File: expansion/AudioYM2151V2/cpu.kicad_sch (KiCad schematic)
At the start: 31 parts, among them J3 JTAG_68K, J4 Serial Out, U10 74LS374, U11 68008, U12 74LS374, U13 74LS148, U14 AS6C4008-55PCN, U15 AT28C256B, U16 XC9536PC44, U17 SC26C92C1A, U9 74LS374, X2 8Mhz, Y1 3.6864Mhz

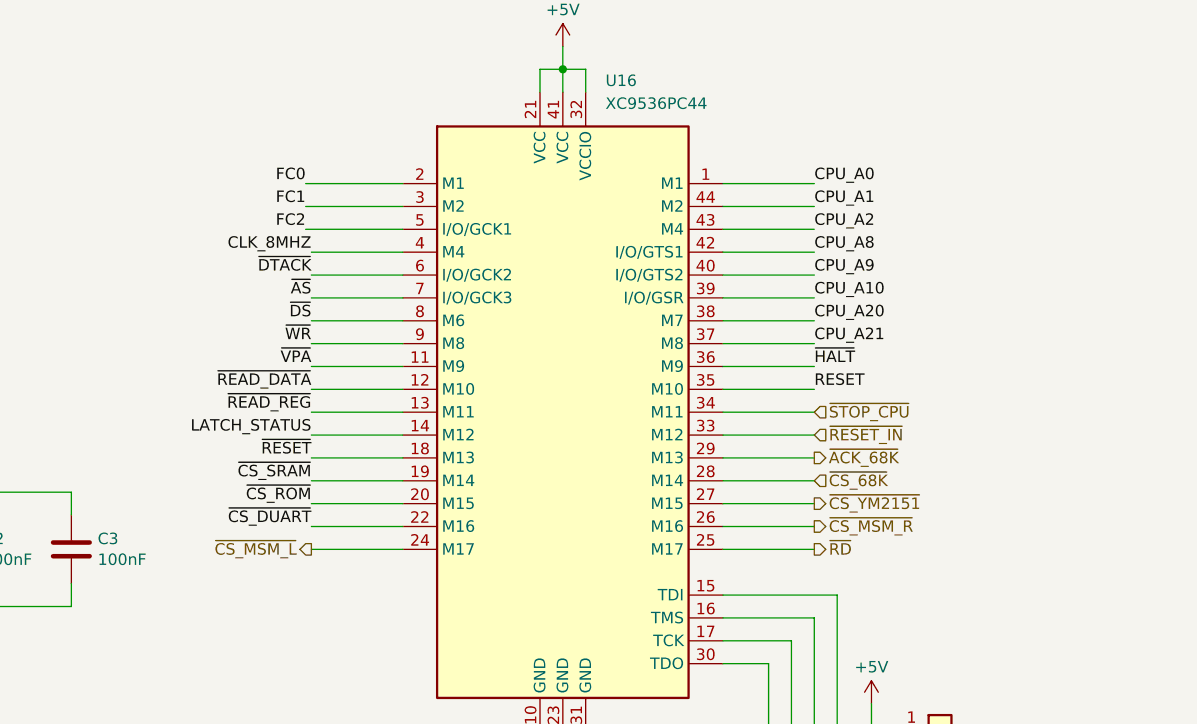
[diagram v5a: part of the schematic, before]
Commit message: Started layout of YM2151
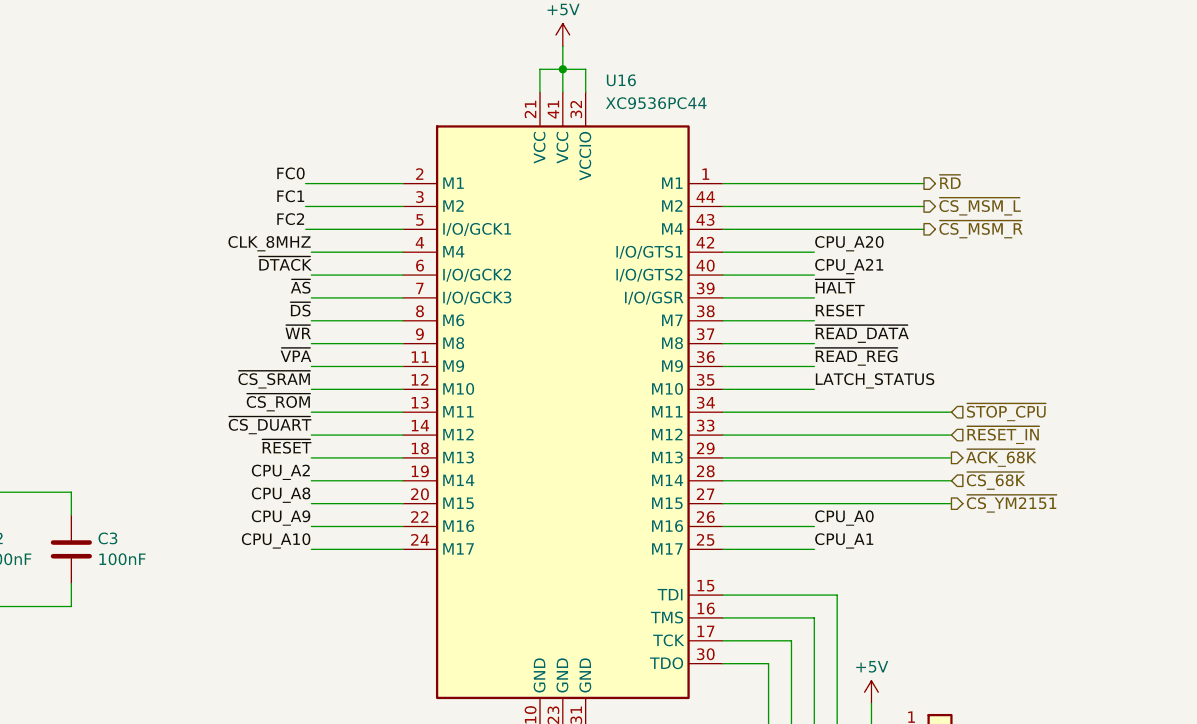
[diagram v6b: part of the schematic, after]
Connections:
- net CPU_A0: now also U16.26 (M16); no longer U16.1 (M1)
- net CPU_A1: now also U16.25 (M17); no longer U16.44 (M2)
- net CPU_A10: now also U16.24 (M17); no longer U16.39 (I/O/GSR)
- net CPU_A2: now also U16.19 (M14); no longer U16.43 (M4)
- net CPU_A20: now also U16.42 (I/O/GTS1); no longer U16.38 (M7)
- net CPU_A21: now also U16.40 (I/O/GTS2); no longer U16.37 (M8)
- net CPU_A8: now also U16.20 (M15); no longer U16.42 (I/O/GTS1)
- net CPU_A9: now also U16.22 (M16); no longer U16.40 (I/O/GTS2)
- net LATCH_STATUS: now also U16.35 (M10); no longer U16.14 (M12)
- net RESET: now also U16.38 (M7); no longer U16.35 (M10)
- net ~{CS_DUART}: now also U16.14 (M12); no longer U16.22 (M16)
- net ~{CS_MSM_L}: now also U16.44 (M2); no longer U16.24 (M17)
- net ~{CS_MSM_R}: now also U16.43 (M4); no longer U16.26 (M16)
- net ~{CS_ROM}: now also U16.13 (M11); no longer U16.20 (M15)
- net ~{CS_SRAM}: now also U16.12 (M10); no longer U16.19 (M14)
- net ~{HALT}: now also U16.39 (I/O/GSR); no longer U16.36 (M9)
- net ~{RD}: now also U16.1 (M1); no longer U16.25 (M17)
- net ~{READ_DATA}: now also U16.37 (M8); no longer U16.12 (M10)
- net ~{READ_REG}: now also U16.36 (M9); no longer U16.13 (M11)
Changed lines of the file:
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@@
     (stroke (width 0) (type default))
   )
-  (wire (pts (xy 353.06 208.28) (xy 363.22 208.28))
+  (wire (pts (xy 353.06 208.28) (xy 378.46 208.28))
     (stroke (width 0) (type default))
   )
@@
     (stroke (width 0) (type default))
   )
-  (wire (pts (xy 353.06 177.8) (xy 363.22 177.8))
+  (wire (pts (xy 353.06 177.8) (xy 375.412 177.8))
     (stroke (width 0) (type default))
   )
@@
     (stroke (width 0) (type default))
   )
-  (wire (pts (xy 353.06 203.2) (xy 363.22 203.2))
+  (wire (pts (xy 353.06 203.2) (xy 378.46 203.2))
     (stroke (width 0) (type default))
   )
@@
     (stroke (width 0) (type default))
   )
-  (wire (pts (xy 353.06 205.74) (xy 363.22 205.74))
+  (wire (pts (xy 353.06 205.74) (xy 378.46 205.74))
     (stroke (width 0) (type default))
   )
@@
     (stroke (width 0) (type default))
   )
-  (wire (pts (xy 353.06 180.34) (xy 363.22 180.34))
+  (wire (pts (xy 353.06 180.34) (xy 375.412 180.34))
     (stroke (width 0) (type default))
   )
@@
     (stroke (width 0) (type default))
   )
-  (wire (pts (xy 353.06 210.82) (xy 363.22 210.82))
+  (wire (pts (xy 353.06 210.82) (xy 378.46 210.82))
     (stroke (width 0) (type default))
   )
@@
     (stroke (width 0) (type default))
   )
-  (wire (pts (xy 353.06 182.88) (xy 363.22 182.88))
+  (wire (pts (xy 353.06 182.88) (xy 375.412 182.88))
     (stroke (width 0) (type default))
   )
@@
     (stroke (width 0) (type default))
   )
-  (wire (pts (xy 353.06 213.36) (xy 363.22 213.36))
+  (wire (pts (xy 353.06 213.36) (xy 378.46 213.36))
     (stroke (width 0) (type default))
   )
@@
     (effects (font (size 1.27 1.27)) (justify left bottom))
   )
-  (label "CPU_A21" (at 363.22 195.58 0) (fields_autoplaced)
+  (label "CPU_A21" (at 363.22 187.96 0) (fields_autoplaced)
     (effects (font (size 1.27 1.27)) (justify left bottom))
   )
@@
     (effects (font (size 1.27 1.27)) (justify right bottom))
   )
-  (label "RESET" (at 363.22 200.66 0) (fields_autoplaced)
+  (label "RESET" (at 363.22 193.04 0) (fields_autoplaced)
     (effects (font (size 1.27 1.27)) (justify left bottom))
   )
@@
     (effects (font (size 1.27 1.27)) (justify right bottom))
   )
-  (label "~{READ_DATA}" (at 307.34 200.66 180) (fields_autoplaced)
-    (effects (font (size 1.27 1.27)) (justify right bottom))
+  (label "~{READ_DATA}" (at 363.22 195.58 0) (fields_autoplaced)
+    (effects (font (size 1.27 1.27)) (justify left bottom))
   )
   (label "CPU_A5" (at 255.651 60.96 180) (fields_autoplaced)
@@
     (effects (font (size 1.27 1.27)) (justify right bottom))
   )
-  (label "~{CS_ROM}" (at 307.34 213.36 180) (fields_autoplaced)
+  (label "~{CS_ROM}" (at 307.34 203.2 180) (fields_autoplaced)
     (effects (font (size 1.27 1.27)) (justify right bottom))
   )
@@
     (effects (font (size 1.27 1.27)) (justify left bottom))
   )
-  (label "CPU_A20" (at 363.22 193.04 0) (fields_autoplaced)
+  (label "CPU_A20" (at 363.22 185.42 0) (fields_autoplaced)
     (effects (font (size 1.27 1.27)) (justify left bottom))
   )
@@
     (effects (font (size 1.27 1.27)) (justify left bottom))
   )
-  (label "~{CS_DUART}" (at 307.34 215.9 180) (fields_autoplaced)
+  (label "~{CS_DUART}" (at 307.34 205.74 180) (fields_autoplaced)
     (effects (font (size 1.27 1.27)) (justify right bottom))
   )
@@
     (effects (font (size 1.27 1.27)) (justify left bottom))
   )
-  (label "CPU_A0" (at 363.22 177.8 0) (fields_autoplaced)
-    (effects (font (size 1.27 1.27)) (justify left bottom))
-  )
-  (label "CPU_A10" (at 363.22 190.5 0) (fields_autoplaced)
-    (effects (font (size 1.27 1.27)) (justify left bottom))
+  (label "CPU_A0" (at 363.22 215.9 0) (fields_autoplaced)
+    (effects (font (size 1.27 1.27)) (justify left bottom))
+  )
+  (label "CPU_A10" (at 307.34 218.44 180) (fields_autoplaced)
+    (effects (font (size 1.27 1.27)) (justify right bottom))
   )
   (label "CPU_D5" (at 325.12 102.87 180) (fields_autoplaced)
@@
     (effects (font (size 1.27 1.27)) (justify left bottom))
   )
-  (label "LATCH_STATUS" (at 307.34 205.74 180) (fields_autoplaced)
-    (effects (font (size 1.27 1.27)) (justify right bottom))
+  (label "LATCH_STATUS" (at 363.22 200.66 0) (fields_autoplaced)
+    (effects (font (size 1.27 1.27)) (justify left bottom))
   )
   (label "CPU_D3" (at 96.52 243.84 0) (fields_autoplaced)
@@
     (effects (font (size 1.27 1.27)) (justify left bottom))
   )
-  (label "CPU_A1" (at 363.22 180.34 0) (fields_autoplaced)
+  (label "CPU_A1" (at 363.22 218.44 0) (fields_autoplaced)
     (effects (font (size 1.27 1.27)) (justify left bottom))
   )
@@
     (effects (font (size 1.27 1.27)) (justify right bottom))
   )
-  (label "CPU_A8" (at 363.22 185.42 0) (fields_autoplaced)
-    (effects (font (size 1.27 1.27)) (justify left bottom))
+  (label "CPU_A8" (at 307.34 213.36 180) (fields_autoplaced)
+    (effects (font (size 1.27 1.27)) (justify right bottom))
   )
   (label "CPU_D0" (at 96.52 236.22 0) (fields_autoplaced)
@@
     (effects (font (size 1.27 1.27)) (justify right bottom))
   )
-  (label "~{HALT}" (at 363.22 198.12 0) (fields_autoplaced)
+  (label "~{HALT}" (at 363.22 190.5 0) (fields_autoplaced)
     (effects (font (size 1.27 1.27)) (justify left bottom))
   )
@@
     (effects (font (size 1.27 1.27)) (justify right bottom))
   )
-  (label "CPU_A9" (at 363.22 187.96 0) (fields_autoplaced)
-    (effects (font (size 1.27 1.27)) (justify left bottom))
+  (label "CPU_A9" (at 307.34 215.9 180) (fields_autoplaced)
+    (effects (font (size 1.27 1.27)) (justify right bottom))
   )
   (label "CPU_A7" (at 255.651 66.04 180) (fields_autoplaced)
@@
     (effects (font (size 1.27 1.27)) (justify left bottom))
   )
-  (label "CPU_A2" (at 363.22 182.88 0) (fields_autoplaced)
-    (effects (font (size 1.27 1.27)) (justify left bottom))
+  (label "CPU_A2" (at 307.34 210.82 180) (fields_autoplaced)
+    (effects (font (size 1.27 1.27)) (justify right bottom))
   )
   (label "CPU_A17" (at 187.071 91.44 180) (fields_autoplaced)
@@
     (effects (font (size 1.27 1.27)) (justify right bottom))
   )
-  (label "~{CS_SRAM}" (at 307.34 210.82 180) (fields_autoplaced)
+  (label "~{CS_SRAM}" (at 307.34 200.66 180) (fields_autoplaced)
     (effects (font (size 1.27 1.27)) (justify right bottom))
   )
@@
     (effects (font (size 1.27 1.27)) (justify right bottom))
   )
-  (label "~{READ_REG}" (at 307.34 203.2 180) (fields_autoplaced)
-    (effects (font (size 1.27 1.27)) (justify right bottom))
+  (label "~{READ_REG}" (at 363.22 198.12 0) (fields_autoplaced)
+    (effects (font (size 1.27 1.27)) (justify left bottom))
   )
   (label "CPU_A18" (at 187.071 93.98 180) (fields_autoplaced)
@@
     (effects (font (size 1.27 1.27)) (justify left bottom))
   )
-  (hierarchical_label "~{CS_MSM_R}" (shape output) (at 363.22 215.9 0) (fields_autoplaced)
+  (hierarchical_label "~{CS_MSM_R}" (shape output) (at 375.412 182.88 0) (fields_autoplaced)
     (effects (font (size 1.27 1.27)) (justify left))
   )
-  (hierarchical_label "~{CS_68K}" (shape input) (at 363.22 210.82 0) (fields_autoplaced)
+  (hierarchical_label "~{CS_68K}" (shape input) (at 378.46 210.82 0) (fields_autoplaced)
     (effects (font (size 1.27 1.27)) (justify left))
   )
@@
     (effects (font (size 1.27 1.27)) (justify left))
   )
-  (hierarchical_label "~{STOP_CPU}" (shape input) (at 363.22 203.2 0) (fields_autoplaced)
+  (hierarchical_label "~{STOP_CPU}" (shape input) (at 378.46 203.2 0) (fields_autoplaced)
     (effects (font (size 1.27 1.27)) (justify left))
   )
@@
     (effects (font (size 1.27 1.27)) (justify right))
   )
-  (hierarchical_label "~{ACK_68K}" (shape output) (at 363.22 208.28 0) (fields_autoplaced)
+  (hierarchical_label "~{ACK_68K}" (shape output) (at 378.46 208.28 0) (fields_autoplaced)
     (effects (font (size 1.27 1.27)) (justify left))
   )
@@
     (effects (font (size 1.27 1.27)) (justify right))
   )
-  (hierarchical_label "~{CS_YM2151}" (shape output) (at 363.22 213.36 0) (fields_autoplaced)
+  (hierarchical_label "~{CS_YM2151}" (shape output) (at 378.46 213.36 0) (fields_autoplaced)
     (effects (font (size 1.27 1.27)) (justify left))
   )
@@
     (effects (font (size 1.27 1.27)) (justify left))
   )
-  (hierarchical_label "~{RESET_IN}" (shape input) (at 363.22 205.74 0) (fields_autoplaced)
+  (hierarchical_label "~{RESET_IN}" (shape input) (at 378.46 205.74 0) (fields_autoplaced)
     (effects (font (size 1.27 1.27)) (justify left))
   )
@@
     (effects (font (size 1.27 1.27)) (justify left))
   )
-  (hierarchical_label "~{RD}" (shape output) (at 363.22 218.44 0) (fields_autoplaced)
+  (hierarchical_label "~{RD}" (shape output) (at 375.412 177.8 0) (fields_autoplaced)
     (effects (font (size 1.27 1.27)) (justify left))
   )
@@
     (effects (font (size 1.27 1.27)) (justify right))
   )
-  (hierarchical_label "~{CS_MSM_L}" (shape output) (at 307.34 218.44 180) (fields_autoplaced)
-    (effects (font (size 1.27 1.27)) (justify right))
+  (hierarchical_label "~{CS_MSM_L}" (shape output) (at 375.412 180.34 0) (fields_autoplaced)
+    (effects (font (size 1.27 1.27)) (justify left))
   )
   (hierarchical_label "MSMSAM1" (shape output) (at 378.46 107.95 0) (fields_autoplaced)

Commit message: YM 2151 changes
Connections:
- net ~{STOP_CPU}: no longer names the net of U16.34 (M11)
- no-connect marks 14 -> 15
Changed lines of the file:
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@@
   (junction (at 335.28 165.1) (diameter 0) (color 0 0 0 0)
+  )
+  (junction (at 309.88 27.94) (diameter 0) (color 0 0 0 0)
   )
   (junction (at 224.155 212.09) (diameter 0) (color 0 0 0 0)
@@
   (no_connect (at 365.76 73.66))
   (no_connect (at 140.335 83.82))
+  (no_connect (at 353.06 203.2))
   (no_connect (at 365.76 95.25))
   (no_connect (at 94.615 86.36))
@@
     (stroke (width 0) (type default))
   )
-  (wire (pts (xy 353.06 177.8) (xy 375.412 177.8))
+  (wire (pts (xy 353.06 177.8) (xy 375.92 177.8))
     (stroke (width 0) (type default))
   )
@@
     (stroke (width 0) (type default))
   )
-  (wire (pts (xy 353.06 203.2) (xy 378.46 203.2))
-    (stroke (width 0) (type default))
-  )
   (wire (pts (xy 141.605 35.56) (xy 155.575 35.56))
     (stroke (width 0) (type default))
@@
     (stroke (width 0) (type default))
   )
+  (bus (pts (xy 309.88 27.94) (xy 317.5 27.94))
+    (stroke (width 0) (type default))
+  )
   (wire (pts (xy 63.5 193.04) (xy 68.58 193.04))
     (stroke (width 0) (type default))
@@
     (stroke (width 0) (type default))
   )
-  (wire (pts (xy 353.06 180.34) (xy 375.412 180.34))
+  (wire (pts (xy 353.06 180.34) (xy 375.92 180.34))
     (stroke (width 0) (type default))
   )
@@
     (stroke (width 0) (type default))
   )
-  (wire (pts (xy 353.06 182.88) (xy 375.412 182.88))
+  (wire (pts (xy 353.06 182.88) (xy 375.92 182.88))
     (stroke (width 0) (type default))
   )
@@
     (effects (font (size 1.27 1.27)) (justify left bottom))
   )
-  (hierarchical_label "~{CS_MSM_R}" (shape output) (at 375.412 182.88 0) (fields_autoplaced)
+  (hierarchical_label "~{CS_MSM_R}" (shape output) (at 375.92 182.88 0) (fields_autoplaced)
+    (effects (font (size 1.27 1.27)) (justify left))
+  )
+  (hierarchical_label "CPU_D[0..7]" (shape bidirectional) (at 317.5 27.94 0) (fields_autoplaced)
     (effects (font (size 1.27 1.27)) (justify left))
   )
@@
     (effects (font (size 1.27 1.27)) (justify left))
   )
-  (hierarchical_label "~{STOP_CPU}" (shape input) (at 378.46 203.2 0) (fields_autoplaced)
-    (effects (font (size 1.27 1.27)) (justify left))
-  )
   (hierarchical_label "LATCH_REG" (shape input) (at 48.26 200.66 180) (fields_autoplaced)
     (effects (font (size 1.27 1.27)) (justify right))
@@
     (effects (font (size 1.27 1.27)) (justify left))
   )
-  (hierarchical_label "~{RD}" (shape output) (at 375.412 177.8 0) (fields_autoplaced)
+  (hierarchical_label "~{RD}" (shape output) (at 375.92 177.8 0) (fields_autoplaced)
     (effects (font (size 1.27 1.27)) (justify left))
   )
@@
     (effects (font (size 1.27 1.27)) (justify right))
   )
-  (hierarchical_label "~{CS_MSM_L}" (shape output) (at 375.412 180.34 0) (fields_autoplaced)
+  (hierarchical_label "~{CS_MSM_L}" (shape output) (at 375.92 180.34 0) (fields_autoplaced)
     (effects (font (size 1.27 1.27)) (justify left))
   )
